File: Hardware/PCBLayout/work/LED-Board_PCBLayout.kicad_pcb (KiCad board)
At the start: 2 copper layers, 100 x 100 mm, 20 parts, among them Q1 BC846, Q2 BC856, U1 L78L05_TO92

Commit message: power supply / power unit
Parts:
- added +12V: MHole, Connector_Pin:Pin_D1.3mm_L11.0mm, F.Cu at (36.0, 24.0)
- added D10: BZV55C3V3, Diode_SMD:D_MiniMELF, F.Cu at (53.3, 78.8)
- added D11: BZV55C3V3, Diode_SMD:D_MiniMELF, F.Cu at (53.3, 82.0)
- added D12: BZV55C3V3, Diode_SMD:D_MiniMELF, F.Cu at (72.3, 78.8)
- added D13: BZV55C3V3, Diode_SMD:D_MiniMELF, F.Cu at (72.3, 82.0)
- added D14: BZV55C3V3, Diode_SMD:D_MiniMELF, F.Cu at (59.6, 78.8)
- added D15: BZV55C3V3, Diode_SMD:D_MiniMELF, F.Cu at (59.6, 82.0)
- added D16: BZV55C3V3, Diode_SMD:D_MiniMELF, F.Cu at (53.3, 85.2)
- added D17: BZV55C3V3, Diode_SMD:D_MiniMELF, F.Cu at (66.0, 85.2)
- added D18: BZV55C3V3, Diode_SMD:D_MiniMELF, F.Cu at (59.6, 85.2)
- added D4: BZV55C3V3, Diode_SMD:D_MiniMELF, F.Cu at (66.0, 82.0)
- added D5: BZV55C3V3, Diode_SMD:D_MiniMELF, F.Cu at (66.0, 78.8)
- added D6: BZV55C3V3, Diode_SMD:D_MiniMELF, F.Cu at (59.6, 88.5)
- added D7: BZV55C3V3, Diode_SMD:D_MiniMELF, F.Cu at (53.3, 88.5)
- added D8: BZV55C3V3, Diode_SMD:D_MiniMELF, F.Cu at (53.3, 95.0)
- added D9: BZV55C3V3, Diode_SMD:D_MiniMELF, F.Cu at (53.3, 91.8)
- added GND: MHole, Connector_Pin:Pin_D1.3mm_L11.0mm, F.Cu at (36.0, 30.0)
- added GND10: MHole, Connector_Pin:Pin_D1.3mm_L11.0mm, F.Cu at (111.4, 79.5)
- added GND11: MHole, Connector_Pin:Pin_D1.3mm_L11.0mm, F.Cu at (92.8, 88.8)
- added GND12: MHole, Connector_Pin:Pin_D1.3mm_L11.0mm, F.Cu at (72.0, 103.8)
- added GND13: MHole, Connector_Pin:Pin_D1.3mm_L11.0mm, F.Cu at (97.4, 79.5)
- added GND14: MHole, Connector_Pin:Pin_D1.3mm_L11.0mm, F.Cu at (76.7, 106.5)
- added GND15: MHole, Connector_Pin:Pin_D1.3mm_L11.0mm, F.Cu at (81.5, 102.1)
- added GND16: MHole, Connector_Pin:Pin_D1.3mm_L11.0mm, F.Cu at (62.2, 110.2)
- added GND2: MHole, Connector_Pin:Pin_D1.3mm_L11.0mm, F.Cu at (76.9, 101.9)
- added GND3: MHole, Connector_Pin:Pin_D1.3mm_L11.0mm, F.Cu at (106.5, 84.1)
- added GND4: MHole, Connector_Pin:Pin_D1.3mm_L11.0mm, F.Cu at (76.4, 111.2)
- added GND5: MHole, Connector_Pin:Pin_D1.3mm_L11.0mm, F.Cu at (106.7, 79.5)
- added GND6: MHole, Connector_Pin:Pin_D1.3mm_L11.0mm, F.Cu at (88.1, 88.5)
- added GND7: MHole, Connector_Pin:Pin_D1.3mm_L11.0mm, F.Cu at (90.8, 98.0)
- added GND8: MHole, Connector_Pin:Pin_D1.3mm_L11.0mm, F.Cu at (76.9, 97.2)
- added GND9: MHole, Connector_Pin:Pin_D1.3mm_L11.0mm, F.Cu at (66.9, 110.5)
- added LED10: MHole, Connector_Pin:Pin_D1.3mm_L11.0mm, F.Cu at (101.8, 84.1)
- added LED11: MHole, Connector_Pin:Pin_D1.3mm_L11.0mm, F.Cu at (97.4, 88.8)
- added LED12: MHole, Connector_Pin:Pin_D1.3mm_L11.0mm, F.Cu at (92.5, 83.9)
- added LED13: MHole, Connector_Pin:Pin_D1.3mm_L11.0mm, F.Cu at (86.2, 102.5)
- added LED14: MHole, Connector_Pin:Pin_D1.3mm_L11.0mm, F.Cu at (97.2, 93.4)
- added LED15: MHole, Connector_Pin:Pin_D1.3mm_L11.0mm, F.Cu at (81.5, 97.5)
- added LED16: MHole, Connector_Pin:Pin_D1.3mm_L11.0mm, F.Cu at (83.2, 92.8)
- added LED2: MHole, Connector_Pin:Pin_D1.3mm_L11.0mm, F.Cu at (71.8, 108.4)
- added LED3: MHole, Connector_Pin:Pin_D1.3mm_L11.0mm, F.Cu at (67.1, 105.8)
- added LED4: MHole, Connector_Pin:Pin_D1.3mm_L11.0mm, F.Cu at (81.3, 106.8)
- added LED5: MHole, Connector_Pin:Pin_D1.3mm_L11.0mm, F.Cu at (87.9, 93.2)
- added LED6: MHole, Connector_Pin:Pin_D1.3mm_L11.0mm, F.Cu at (102.1, 79.5)
- added LED7: MHole, Connector_Pin:Pin_D1.3mm_L11.0mm, F.Cu at (92.5, 93.4)
- added LED8: MHole, Connector_Pin:Pin_D1.3mm_L11.0mm, F.Cu at (97.2, 84.1)
- added LED9: MHole, Connector_Pin:Pin_D1.3mm_L11.0mm, F.Cu at (86.2, 97.8)
- added Q10: BC846, Package_TO_SOT_SMD:SOT-23, F.Cu at (87.8, 79.3)
- added Q11: BC846, Package_TO_SOT_SMD:SOT-23, F.Cu at (83.4, 88.2)
- added Q12: BC846, Package_TO_SOT_SMD:SOT-23, F.Cu at (67.2, 101.2)
- added Q13: BC846, Package_TO_SOT_SMD:SOT-23, F.Cu at (92.6, 79.3)
- added Q14: BC846, Package_TO_SOT_SMD:SOT-23, F.Cu at (67.2, 96.8)
- added Q15: BC846, Package_TO_SOT_SMD:SOT-23, F.Cu at (57.5, 107.8)
- added Q16: BC846, Package_TO_SOT_SMD:SOT-23, F.Cu at (72.1, 94.8)
- added Q17: BC856, Package_TO_SOT_SMD:SOT-23, F.Cu at (78.5, 88.2)
- added Q18: BC856, Package_TO_SOT_SMD:SOT-23, F.Cu at (62.4, 101.2)
- added Q19: BC856, Package_TO_SOT_SMD:SOT-23, F.Cu at (52.6, 103.3)
- added Q2: BC856, Package_TO_SOT_SMD:SOT-23, F.Cu at (73.6, 90.3)
- added Q20: BC856, Package_TO_SOT_SMD:SOT-23, F.Cu at (57.5, 112.2)
- added Q21: BC856, Package_TO_SOT_SMD:SOT-23, F.Cu at (87.8, 83.8)
- added Q22: BC856, Package_TO_SOT_SMD:SOT-23, F.Cu at (63.8, 92.3)
- added Q23: BC856, Package_TO_SOT_SMD:SOT-23, F.Cu at (52.6, 107.8)
- added Q24: BC856, Package_TO_SOT_SMD:SOT-23, F.Cu at (78.5, 92.7)
- added Q25: BC846, Package_TO_SOT_SMD:SOT-23, F.Cu at (71.6, 85.8)
- added Q26: BC846, Package_TO_SOT_SMD:SOT-23, F.Cu at (57.5, 103.3)
- added Q27: BC846, Package_TO_SOT_SMD:SOT-23, F.Cu at (58.9, 92.3)
- added Q28: BC846, Package_TO_SOT_SMD:SOT-23, F.Cu at (78.0, 83.8)
- added Q29: BC846, Package_TO_SOT_SMD:SOT-23, F.Cu at (82.9, 83.8)
- added Q3: BC856, Package_TO_SOT_SMD:SOT-23, F.Cu at (72.1, 99.2)
- added Q30: BC846, Package_TO_SOT_SMD:SOT-23, F.Cu at (52.6, 112.2)
- added Q31: BC846, Package_TO_SOT_SMD:SOT-23, F.Cu at (52.6, 98.8)
- added Q32: BC846, Package_TO_SOT_SMD:SOT-23, F.Cu at (82.9, 79.3)
- added Q4: BC856, Package_TO_SOT_SMD:SOT-23, F.Cu at (62.4, 105.7)
- added Q5: BC856, Package_TO_SOT_SMD:SOT-23, F.Cu at (68.7, 90.3)
- added Q6: BC856, Package_TO_SOT_SMD:SOT-23, F.Cu at (57.5, 98.8)
- added Q7: BC856, Package_TO_SOT_SMD:SOT-23, F.Cu at (78.0, 79.3)
- added Q8: BC856, Package_TO_SOT_SMD:SOT-23, F.Cu at (62.4, 96.8)
- added R10: R_Small, Resistor_SMD:R_0201_0603Metric_Pad0.64x0.40mm_HandSolder, F.Cu at (97.4, 96.6)
- added R11: R_Small, Resistor_SMD:R_0201_0603Metric_Pad0.64x0.40mm_HandSolder, F.Cu at (104.0, 89.0)
- added R12: R_Small, Resistor_SMD:R_0201_0603Metric_Pad0.64x0.40mm_HandSolder, F.Cu at (64.1, 113.7)
- added R13: R_Small, Resistor_SMD:R_0201_0603Metric_Pad0.64x0.40mm_HandSolder, F.Cu at (89.9, 103.0)
- added R14: R_Small, Resistor_SMD:R_0201_0603Metric_Pad0.64x0.40mm_HandSolder, F.Cu at (101.2, 90.8)
- added R15: R_Small, Resistor_SMD:R_0201_0603Metric_Pad0.64x0.40mm_HandSolder, F.Cu at (110.2, 82.7)
- added R16: R_Small, Resistor_SMD:R_0201_0603Metric_Pad0.64x0.40mm_HandSolder, F.Cu at (92.7, 101.2)
- added R17: R_Small, Resistor_SMD:R_0201_0603Metric_Pad0.64x0.40mm_HandSolder, F.Cu at (94.6, 98.3)
- added R18: R_Small, Resistor_SMD:R_0201_0603Metric_Pad0.64x0.40mm_HandSolder, F.Cu at (80.2, 111.7)
- added R19: R_Small, Resistor_SMD:R_0201_0603Metric_Pad0.64x0.40mm_HandSolder, F.Cu at (115.1, 78.0)
- added R2: R_Small, Resistor_SMD:R_0201_0603Metric_Pad0.64x0.40mm_HandSolder, F.Cu at (72.5, 113.3)
- added R20: R_Small, Resistor_SMD:R_0201_0603Metric_Pad0.64x0.40mm_HandSolder, F.Cu at (69.7, 113.7)
- added R21: R_Small, Resistor_SMD:R_0201_0603Metric_Pad0.64x0.40mm_HandSolder, F.Cu at (70.6, 111.6)
- added R22: R_Small, Resistor_SMD:R_0201_0603Metric_Pad0.64x0.40mm_HandSolder, F.Cu at (104.0, 87.3)
- added R23: R_Small, Resistor_SMD:R_0201_0603Metric_Pad0.64x0.40mm_HandSolder, F.Cu at (101.2, 87.3)
- added R24: R_Small, Resistor_SMD:R_0201_0603Metric_Pad0.64x0.40mm_HandSolder, F.Cu at (106.8, 87.3)
- added R25: R_Small, Resistor_SMD:R_0201_0603Metric_Pad0.64x0.40mm_HandSolder, F.Cu at (64.2, 87.8)
- added R26: R_Small, Resistor_SMD:R_0201_0603Metric_Pad0.64x0.40mm_HandSolder, F.Cu at (57.9, 95.5)
- added R27: R_Small, Resistor_SMD:R_0201_0603Metric_Pad0.64x0.40mm_HandSolder, F.Cu at (85.0, 107.5)
- added R28: R_Small, Resistor_SMD:R_0201_0603Metric_Pad0.64x0.40mm_HandSolder, F.Cu at (61.3, 113.5)
- added R29: R_Small, Resistor_SMD:R_0201_0603Metric_Pad0.64x0.40mm_HandSolder, F.Cu at (67.7, 93.4)
- added R3: R_Small, Resistor_SMD:R_0201_0603Metric_Pad0.64x0.40mm_HandSolder, F.Cu at (87.8, 105.7)
- added R30: R_Small, Resistor_SMD:R_0201_0603Metric_Pad0.64x0.40mm_HandSolder, F.Cu at (101.2, 89.0)
- added R31: R_Small, Resistor_SMD:R_0201_0603Metric_Pad0.64x0.40mm_HandSolder, F.Cu at (85.0, 105.7)
- added R32: R_Small, Resistor_SMD:R_0201_0603Metric_Pad0.64x0.40mm_HandSolder, F.Cu at (89.9, 101.2)
- added R4: R_Small, Resistor_SMD:R_0201_0603Metric_Pad0.64x0.40mm_HandSolder, F.Cu at (80.2, 110.0)
- added R5: R_Small, Resistor_SMD:R_0201_0603Metric_Pad0.64x0.40mm_HandSolder, F.Cu at (94.6, 96.6)
- added R6: R_Small, Resistor_SMD:R_0201_0603Metric_Pad0.64x0.40mm_HandSolder, F.Cu at (80.2, 113.5)
- added R7: R_Small, Resistor_SMD:R_0201_0603Metric_Pad0.64x0.40mm_HandSolder, F.Cu at (83.0, 110.0)
- added R8: R_Small, Resistor_SMD:R_0201_0603Metric_Pad0.64x0.40mm_HandSolder, F.Cu at (66.9, 113.7)
- moved R1 24.8 mm to (34.4, 36.5), turned to 180 degrees
- moved D3 16.8 mm to (34.5, 40.5), turned to 90 degrees
- moved GND1 16.5 mm to (25.9, 43.0)
- moved LED1 16.5 mm to (25.9, 38.0)
- moved Q1 16.5 mm to (30.9, 38.0)
- moved Q9 16.5 mm to (30.9, 43.0)
- moved R9 10.3 mm to (34.4, 44.5), turned to 180 degrees
- moved C1 6.92 mm to (43.1, 29.7)
- moved C2 6.92 mm to (48.9, 28.9)
- moved C3 6.92 mm to (56.9, 28.9)
- moved C4 6.92 mm to (60.2, 29.7)
- moved D1 6.92 mm to (54.8, 24.0)
- moved D2 6.92 mm to (51.0, 24.0)
- moved U1 6.92 mm to (54.2, 29.0)
- renumbered D2 to D1, D1 to D2, Q2 to Q1, Q1 to Q9, R2 to R1, R1 to R9
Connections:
- net Net-(C3-Pad1) renamed +5V
- D2 pad 2: +12V -> Net-(+12V1-Pad1)
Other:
- board text added: "LED-Board V2.0"
- board text removed: "LED-Board V1.1"

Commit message: power unit
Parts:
- moved R21 80.0 mm to (113.4, 44.0)
- moved GND3 79.6 mm to (27.0, 89.0)
- moved Q30 69.9 mm to (109.0, 71.0)
- moved D14 65.3 mm to (116.0, 67.0), turned to -90 degrees
- moved D13 64.0 mm to (114.5, 49.0), turned to -90 degrees
- moved LED2 63.8 mm to (27.0, 63.0)
- moved Q23 62.4 mm to (109.0, 81.0), turned to 180 degrees
- moved R11 61.5 mm to (42.5, 90.0)
- moved R29 61.0 mm to (115.0, 55.0)
- moved GND5 60.8 mm to (52.0, 53.0)
- moved R10 60.4 mm to (42.0, 72.5)
- moved LED5 60.1 mm to (52.0, 45.0)
- moved LED13 59.6 mm to (102.0, 45.0)
- moved R5 58.9 mm to (67.0, 44.5)
- moved R2 58.9 mm to (42.0, 63.0)
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- renumbered +12V to +12V_Input1, D3 to D1, D12 to D10, D13 to D11, D14 to D12, D15 to D13, D16 to D14, D17 to D15, D18 to D16, D1 to D17, D2 to D18, D4 to D2, D5 to D3, D6 to D4, D7 to D5, D8 to D6, D9 to D7, D10 to D8, D11 to D9, GND to GND_Input1

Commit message: power unit
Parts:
- added J1: AVR-ISP-6, Connector_JAE:JAE_LY20-6P-DT1_2x03_P2.00mm_Vertical, F.Cu at (99.0, 116.5)
- added RX1: MHole, Connector_Pin:Pin_D1.3mm_L11.0mm, F.Cu at (111.5, 31.0)
- added TX1: MHole, Connector_Pin:Pin_D1.3mm_L11.0mm, F.Cu at (111.5, 36.0)
- added U2: ATmega48-20P, Package_DIP:DIP-28_W7.62mm, F.Cu at (68.5, 33.8)
- moved +12V_1 10.3 mm to (28.5, 31.0)
- moved GND_1 9.60 mm to (28.5, 36.0)
- moved C1 8.01 mm to (35.2, 30.7)
- moved C2 8.01 mm to (41.0, 29.9)
- moved C3 8.01 mm to (49.0, 29.9)
- moved C4 8.01 mm to (52.3, 30.7)
- moved D17 8.01 mm to (46.9, 25.0)
- moved D18 8.01 mm to (43.0, 25.0)
- moved U1 8.01 mm to (46.3, 30.0)
- moved R16 3.20 mm to (64.5, 108.0)
- moved R13 3.00 mm to (64.5, 54.0)
- moved R28 2.92 mm to (89.5, 108.0)
- moved R7 2.73 mm to (64.5, 80.0)
- moved D7 2.69 mm to (64.5, 85.0)
- moved R30 2.69 mm to (114.5, 72.0)
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- renumbered +12V_Input1 to +12V_1, GND_Input1 to GND_1

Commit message: Circuit board layout created
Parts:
- added C5: 100n, Capacitor_SMD:C_0201_0603Metric_Pad0.64x0.40mm_HandSolder, F.Cu at (65.4, 24.0)
- added C6: 100n, Capacitor_SMD:C_0201_0603Metric_Pad0.64x0.40mm_HandSolder, F.Cu at (64.0, 36.0)
- added C7: 100n, Capacitor_SMD:C_0201_0603Metric_Pad0.64x0.40mm_HandSolder, F.Cu at (68.0, 24.0)
- added C8: 1u, Capacitor_SMD:C_0201_0603Metric_Pad0.64x0.40mm_HandSolder, F.Cu at (48.0, 37.0)
- added GND17: MHole, Connector_Pin:Pin_D1.3mm_L11.0mm, F.Cu at (35.0, 30.0)
- added R33: 10k, Resistor_SMD:R_0201_0603Metric_Pad0.64x0.40mm_HandSolder, F.Cu at (52.0, 37.0)
- C1, C4: value C -> 10u
- C2, C3: value C_Small -> 100n
- J1: footprint Connector_JAE:JAE_LY20-6P-DT1_2x03_P2.00mm_Vertical -> Connector_IDC:IDC-Header_2x03_P2.54mm_Vertical
- moved C1 91.8 mm to (72.2, 114.7), turned to 180 degrees
- moved C2 90.8 mm to (75.4, 113.9)
- moved C3 90.8 mm to (83.4, 113.9)
- moved C4 90.8 mm to (86.7, 114.7)
- moved D17 90.8 mm to (81.3, 109.0)
- moved D18 90.8 mm to (77.5, 109.0)
- moved U1 90.8 mm to (80.7, 114.0)
- moved J1 85.7 mm to (99.5, 30.8)
- moved +12V_1 78.3 mm to (35.0, 109.0)
- moved GND_1 78.3 mm to (35.0, 114.0)
- moved TX1 77.3 mm to (35.0, 25.0)
- moved RX1 76.6 mm to (35.0, 35.0)
- moved U2 20.5 mm to (48.0, 33.8)
- moved D12 5.50 mm to (89.5, 97.5), turned to 90 degrees
- moved D16 5.50 mm to (114.5, 97.5), turned to 90 degrees
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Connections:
- net Net-(RX1-Pad1) renamed RX
- net Net-(TX1-Pad1) renamed TX
- C3 pad 1: +5V -> VCC
- C4 pad 1: +5V -> VCC
- D17 pad 2: +5V -> VCC
- Q10 pad 1: OUT2 -> LED2
- Q11 pad 1: OUT3 -> LED3
- Q12 pad 1: OUT4 -> LED4
- Q13 pad 1: OUT5 -> LED5
- Q14 pad 1: OUT6 -> LED6
- Q15 pad 1: OUT7 -> LED7
- Q16 pad 1: OUT8 -> LED8
- Q25 pad 1: OUT9 -> LED9
- Q26 pad 1: OUT10 -> LED10
- Q27 pad 1: OUT11 -> LED11
- Q28 pad 1: OUT12 -> LED12
- Q29 pad 1: OUT13 -> LED13
- Q30 pad 1: OUT14 -> LED14
- Q31 pad 1: OUT15 -> LED15
- Q32 pad 1: OUT16 -> LED16
- Q9 pad 1: OUT1 -> LED1
- U1 pad 1: +5V -> VCC
- U2 pad 1: unconnected-(U2-Pad1) -> RESET
- U2 pad 10: unconnected-(U2-Pad10) -> LED12
- U2 pad 11: unconnected-(U2-Pad11) -> LED11
- U2 pad 12: unconnected-(U2-Pad12) -> LED10
- U2 pad 13: unconnected-(U2-Pad13) -> LED9
- U2 pad 14: unconnected-(U2-Pad14) -> LED16
- U2 pad 15: unconnected-(U2-Pad15) -> LED15
- U2 pad 16: unconnected-(U2-Pad16) -> SS
- U2 pad 17: unconnected-(U2-Pad17) -> MOSI
- U2 pad 18: unconnected-(U2-Pad18) -> MISO
- U2 pad 19: unconnected-(U2-Pad19) -> SCK
- U2 pad 20: unconnected-(U2-Pad20) -> VCC
- U2 pad 21: unconnected-(U2-Pad21) -> VCC
- U2 pad 22: Net-(U2-Pad22) -> GND
- U2 pad 23: unconnected-(U2-Pad23) -> LED14
- U2 pad 24: unconnected-(U2-Pad24) -> LED13
- U2 pad 25: unconnected-(U2-Pad25) -> LED1
- U2 pad 26: unconnected-(U2-Pad26) -> LED2
- U2 pad 27: unconnected-(U2-Pad27) -> LED3
- U2 pad 28: unconnected-(U2-Pad28) -> LED4
- U2 pad 4: unconnected-(U2-Pad4) -> LED5
- U2 pad 5: unconnected-(U2-Pad5) -> LED6
- U2 pad 6: unconnected-(U2-Pad6) -> LED7
- U2 pad 7: unconnected-(U2-Pad7) -> VCC
- U2 pad 8: Net-(U2-Pad22) -> GND
- U2 pad 9: unconnected-(U2-Pad9) -> LED8
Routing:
- net +12V: track 0.00 -> 437.0 mm
- net VCC: track 0.00 -> 206.7 mm, vias 0 -> 1
- net LED16: track 0.00 -> 87.9 mm, vias 0 -> 1
- net LED4: track 0.00 -> 87.2 mm, vias 0 -> 1
- net LED14: track 0.00 -> 84.9 mm, vias 0 -> 1
- net LED15: track 0.00 -> 78.6 mm, vias 0 -> 1
- net LED12: track 0.00 -> 77.1 mm, vias 0 -> 1
- net LED3: track 0.00 -> 76.1 mm, vias 0 -> 1
- net LED8: track 0.00 -> 71.5 mm, vias 0 -> 1
- net LED13: track 0.00 -> 70.3 mm, vias 0 -> 1
- net RESET: track 0.00 -> 65.8 mm
- net LED2: track 0.00 -> 63.3 mm, vias 0 -> 1
- net LED11: track 0.00 -> 56.7 mm, vias 0 -> 1
- net LED7: track 0.00 -> 51.3 mm, vias 0 -> 1
- net LED1: track 0.00 -> 50.5 mm, vias 0 -> 1
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
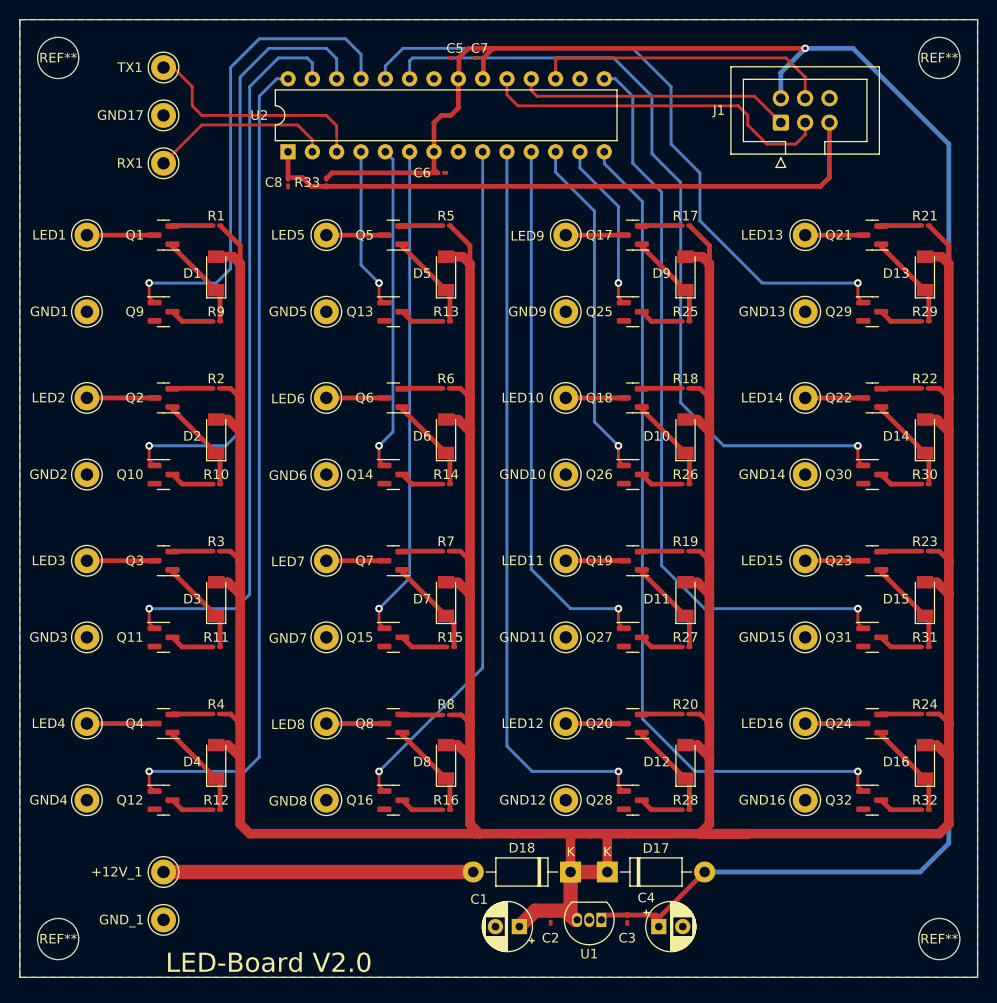
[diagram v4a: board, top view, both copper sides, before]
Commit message: Fuse / Power OK LED
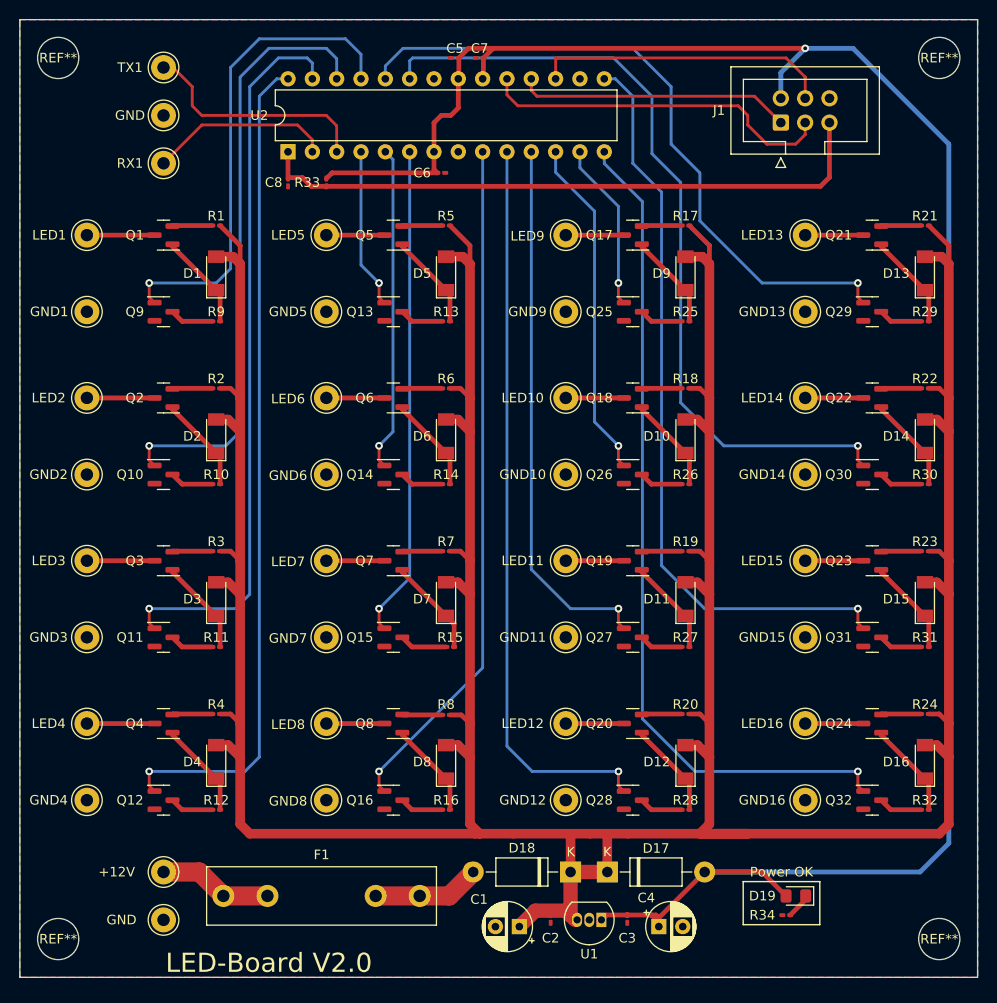
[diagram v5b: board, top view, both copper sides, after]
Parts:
- added D19: LED, Diode_SMD:D_0805_2012Metric_Pad1.15x1.40mm_HandSolder, F.Cu at (101.0, 111.5)
- added F1: 1A, Fuse:Fuseholder_Littelfuse_100_series_5x20mm, F.Cu at (41.2, 111.5)
- added R34: 333, Resistor_SMD:R_0201_0603Metric_Pad0.64x0.40mm_HandSolder, F.Cu at (100.0, 113.5)
- renumbered +12V_1 to +12V, GND_1 to GND, GND17 to GND
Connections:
- D18 pad 2: Net-(+12V_1-Pad1) -> Net-(D18-Pad2)
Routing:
- net Net-(+12V_1-Pad1): track 32.8 -> 11.9 mm
- net Net-(D18-Pad2): track 0.00 -> 11.6 mm
- net VCC: track 206.7 -> 216.3 mm
- net Net-(D19-Pad1): track 0.00 -> 2.67 mm
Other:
- board text added: "Power OK"

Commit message: Circuit board layout created
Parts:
- moved C7 1.12 mm to (68.5, 23.0), turned to 90 degrees
- moved C5 1.00 mm to (65.5, 23.0), turned to 90 degrees
- moved C3 0.58 mm to (84.0, 113.9)
- moved C2 0.42 mm to (75.0, 113.9)
- renumbered REF** to 1, REF** to 2, REF** to 3, REF** to 4
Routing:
- net LED10: track 35.7 -> 48.3 mm
- net LED9: track 17.7 -> 29.2 mm
- net LED11: track 56.7 -> 67.7 mm
- net LED12: track 77.1 -> 87.0 mm
- net LED13: track 70.3 -> 79.9 mm
- net LED14: track 84.9 -> 91.4 mm
- net LED15: track 78.6 -> 84.9 mm
- net LED8: track 71.5 -> 74.4 mm
- net LED1: track 50.5 -> 52.8 mm
- net LED16: track 87.9 -> 90.0 mm
- net LED4: track 87.2 -> 85.6 mm
- net LED2: track 63.3 -> 64.4 mm
- net LED3: track 76.1 -> 75.0 mm
- net VCC: track 216.3 -> 215.4 mm
